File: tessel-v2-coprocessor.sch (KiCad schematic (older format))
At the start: 12 parts

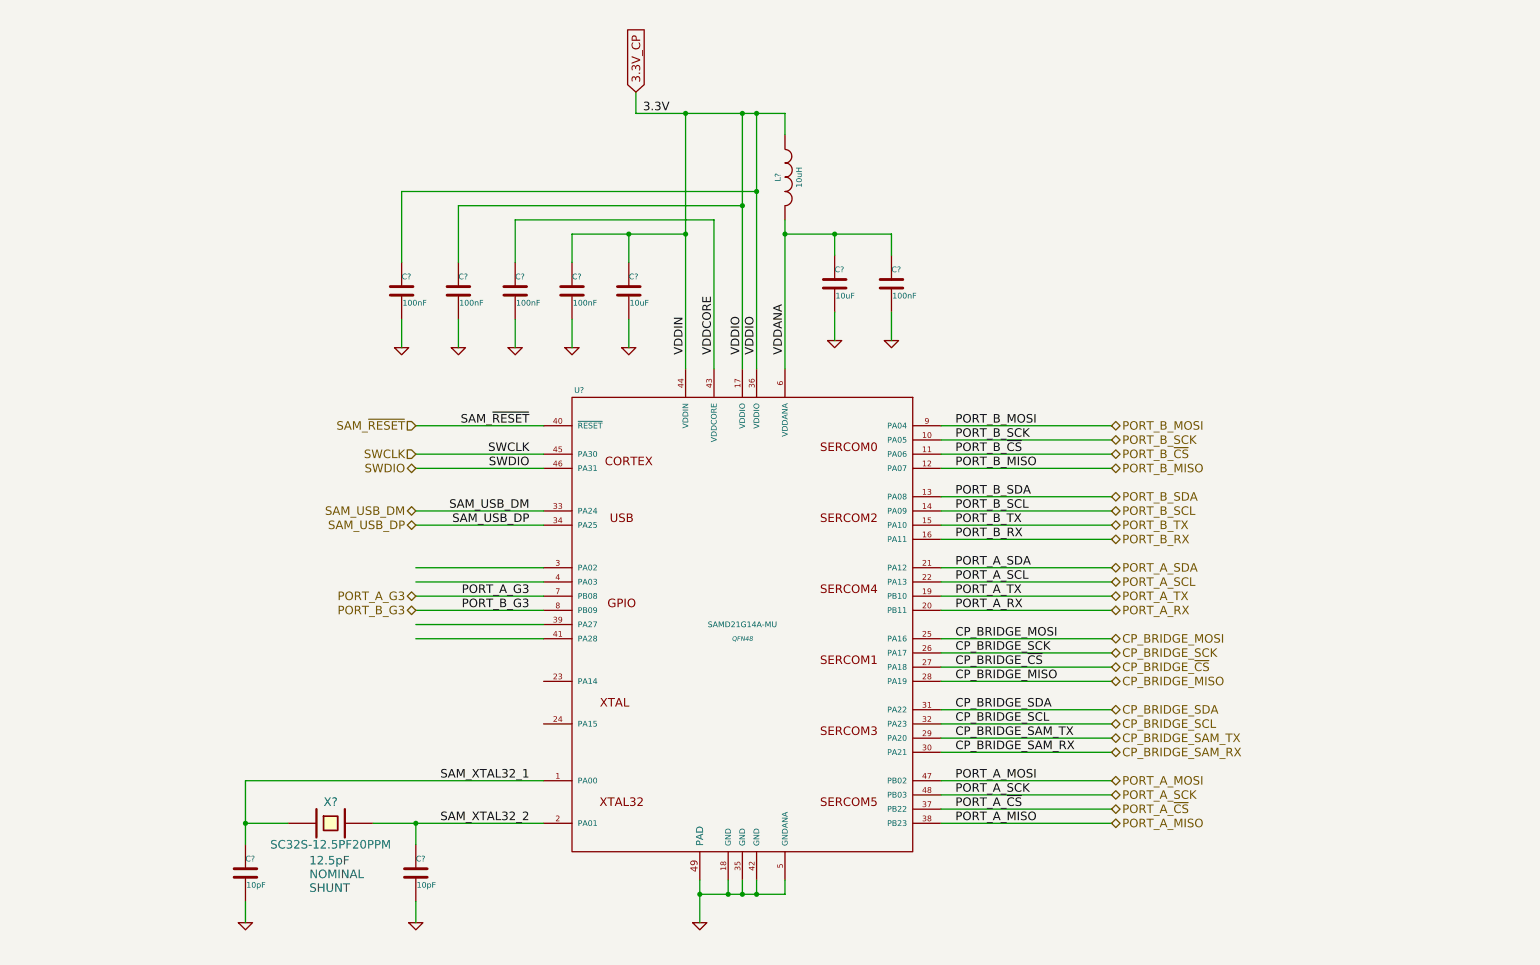
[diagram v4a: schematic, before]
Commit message: labels and series R for MT comms
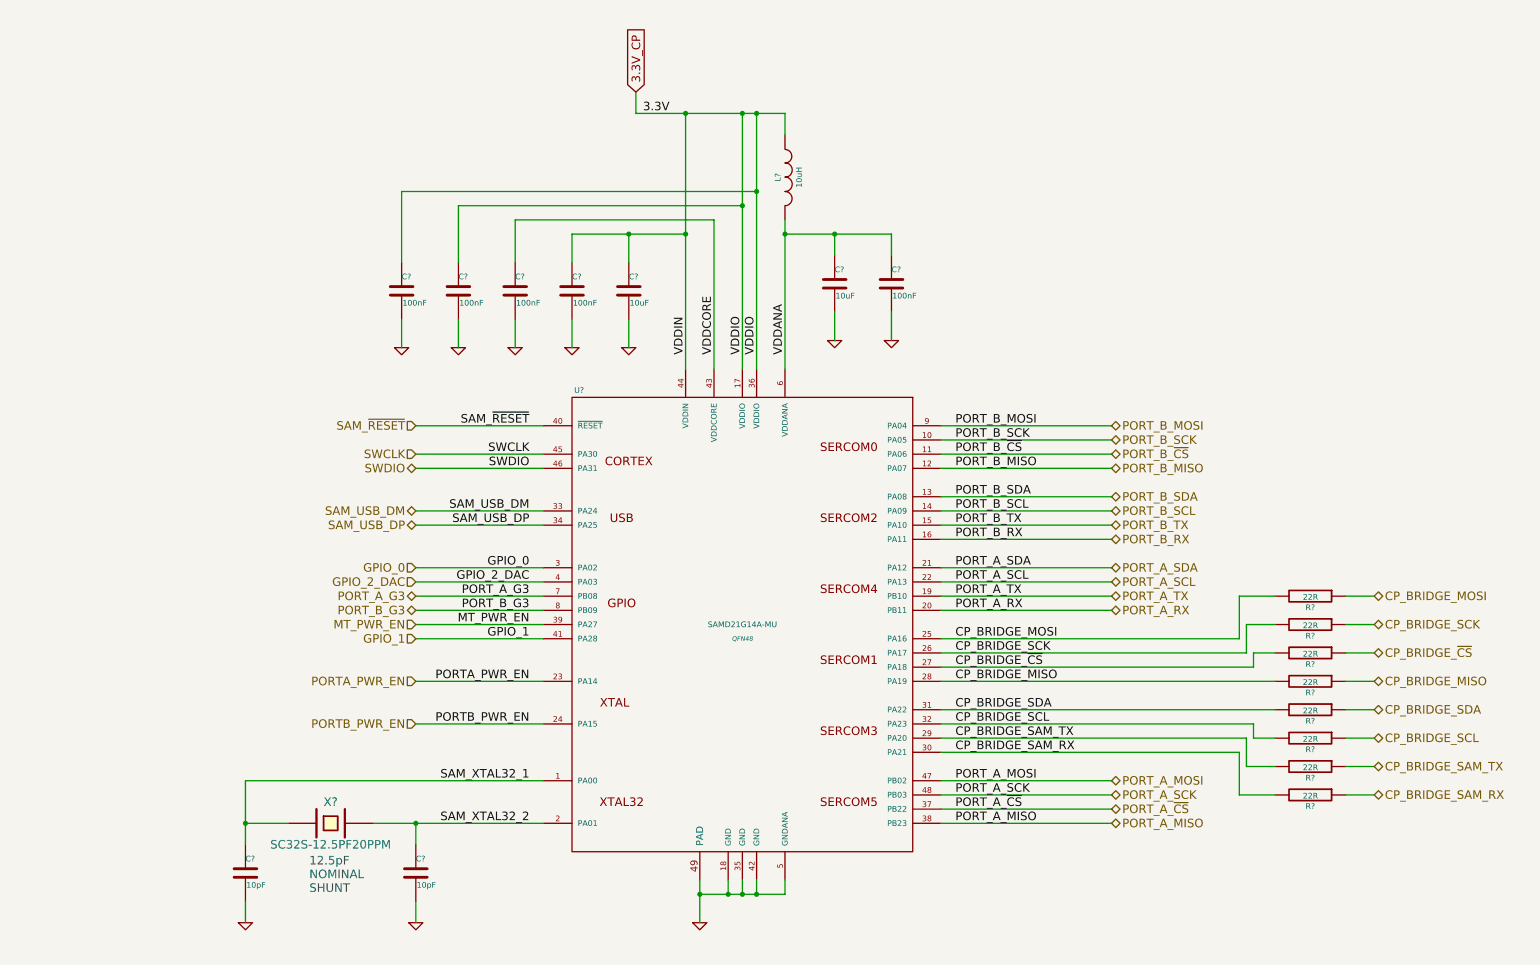
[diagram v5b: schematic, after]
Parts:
- added R? (x8): 22R, symbol R
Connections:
- net labels added: GPIO_0, GPIO_1, GPIO_2_DAC, MT_PWR_EN, PORTA_PWR_EN, PORTB_PWR_EN
- wire segments 90 -> 97
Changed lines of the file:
@@
 Text HLabel 10900 5900 2    60   BiDi ~ 0
 PORT_A_RX
-Text HLabel 10900 6100 2    60   BiDi ~ 0
+Text HLabel 12750 5800 2    60   BiDi ~ 0
 CP_BRIDGE_MOSI
-Text HLabel 10900 6200 2    60   BiDi ~ 0
+Text HLabel 12750 6000 2    60   BiDi ~ 0
 CP_BRIDGE_SCK
-Text HLabel 10900 6300 2    60   BiDi ~ 0
+Text HLabel 12750 6200 2    60   BiDi ~ 0
 CP_BRIDGE_~CS
-Text HLabel 10900 6400 2    60   BiDi ~ 0
+Text HLabel 12750 6400 2    60   BiDi ~ 0
 CP_BRIDGE_MISO
-Text HLabel 10900 6600 2    60   BiDi ~ 0
+Text HLabel 12750 6600 2    60   BiDi ~ 0
 CP_BRIDGE_SDA
-Text HLabel 10900 6700 2    60   BiDi ~ 0
+Text HLabel 12750 6800 2    60   BiDi ~ 0
 CP_BRIDGE_SCL
-Text HLabel 10900 6800 2    60   BiDi ~ 0
+Text HLabel 12750 7000 2    60   BiDi ~ 0
 CP_BRIDGE_SAM_TX
-Text HLabel 10900 6900 2    60   BiDi ~ 0
+Text HLabel 12750 7200 2    60   BiDi ~ 0
 CP_BRIDGE_SAM_RX
 Text HLabel 10900 7100 2    60   BiDi ~ 0
@@
 Connection ~ 7900 2400
 Wire Wire Line
-	7900 2400 7900 3250
-Wire Wire Line
-	7900 3250 7900 4200
+	7900 2400 7900 4200
 Connection ~ 8300 3050
 Connection ~ 8300 2400
@@
 Connection ~ 8400 2400
 Wire Wire Line
-	8400 2400 8400 2950
-Wire Wire Line
-	8400 2950 8400 4200
+	8400 2400 8400 4200
 Wire Wire Line
 	7550 2400 7550 2250
@@
 	8300 3050 6300 3050
 Wire Wire Line
-	8300 2400 8300 3050
-Wire Wire Line
-	8300 3050 8300 4200
+	8300 2400 8300 4200
 Wire Wire Line
 	8100 3150 8100 4200
@@
 	7100 3250 7100 3450
 Wire Wire Line
-	7100 3250 7500 3250
-Wire Wire Line
-	7500 3250 7900 3250
+	7100 3250 7900 3250
 Connection ~ 8600 3250
 Connection ~ 8950 3250
@@
 	8950 3250 8950 3400
 Wire Wire Line
-	8600 3250 8950 3250
-Wire Wire Line
-	8950 3250 9350 3250
-Wire Wire Line
-	8600 3150 8600 3250
-Wire Wire Line
-	8600 3250 8600 4200
+	8600 3250 9350 3250
+Wire Wire Line
+	8600 3150 8600 4200
 Wire Wire Line
 	4800 7950 4800 8100
@@
 	4800 7400 5100 7400
 Wire Wire Line
-	4800 7100 4800 7400
-Wire Wire Line
-	4800 7400 4800 7550
+	4800 7100 4800 7550
 Wire Wire Line
 	9700 7100 10900 7100
@@
 	9700 7200 10900 7200
 Wire Wire Line
-	9700 6900 10900 6900
-Wire Wire Line
-	9700 6800 10900 6800
-Wire Wire Line
-	9700 6700 10900 6700
-Wire Wire Line
-	9700 6600 10900 6600
-Wire Wire Line
-	9700 6400 10900 6400
-Wire Wire Line
-	9700 6300 10900 6300
-Wire Wire Line
-	9700 6200 10900 6200
-Wire Wire Line
-	9700 6100 10900 6100
+	9700 6400 12050 6400
+Wire Wire Line
+	9700 6300 11900 6300
+Wire Wire Line
+	9700 6200 11850 6200
+Wire Wire Line
+	9700 6100 11800 6100
 Wire Wire Line
 	9700 5900 10900 5900
@@
 	9700 4600 10900 4600
 Wire Wire Line
-	5700 7400 6000 7400
-Wire Wire Line
-	6000 7400 6900 7400
+	5700 7400 6900 7400
 Wire Wire Line
 	4800 7100 6900 7100
@@
 	6900 4600 6000 4600
 Wire Wire Line
-	7550 2400 7900 2400
-Wire Wire Line
-	7900 2400 8300 2400
-Wire Wire Line
-	8300 2400 8400 2400
-Wire Wire Line
-	8400 2400 8600 2400
+	7550 2400 8600 2400
 Wire Wire Line
 	7500 3450 7500 3250
@@
 $EndComp
 Wire Wire Line
-	8000 7800 8000 7900
-Wire Wire Line
-	8000 7900 8000 8100
-Wire Wire Line
-	8000 7900 8200 7900
-Wire Wire Line
-	8200 7900 8300 7900
-Wire Wire Line
-	8300 7900 8400 7900
-Wire Wire Line
-	8400 7900 8600 7900
+	8000 7800 8000 8100
+Wire Wire Line
+	8000 7900 8600 7900
 Wire Wire Line
 	8200 7900 8200 7800
@@
 Text GLabel 7550 2250 1    60   Input ~ 0
 3.3V_CP
+Text HLabel 6000 6400 0    60   Input ~ 0
+PORTA_PWR_EN
+Text HLabel 6000 6700 0    60   Input ~ 0
+PORTB_PWR_EN
+Text HLabel 6000 6000 0    60   Input ~ 0
+MT_PWR_EN
+$Comp
+L R R?
+U 1 1 54912B30
+P 12300 6200
+F 0 "R?" V 12380 6200 40  0000 C CNN
+F 1 "22R" V 12307 6201 40  0000 C CNN
+F 2 "" V 12230 6200 30  0000 C CNN
+F 3 "" H 12300 6200 30  0000 C CNN
+	1    12300 6200
+	0    1    1    0
+$EndComp
+$Comp
+L R R?
+U 1 1 54912C7C
+P 12300 6400
+F 0 "R?" V 12380 6400 40  0000 C CNN
+F 1 "22R" V 12307 6401 40  0000 C CNN
+F 2 "" V 12230 6400 30  0000 C CNN
+F 3 "" H 12300 6400 30  0000 C CNN
+	1    12300 6400
+	0    1    1    0
+$EndComp
+$Comp
+L R R?
+U 1 1 54912D2C
+P 12300 5800
+F 0 "R?" V 12380 5800 40  0000 C CNN
+F 1 "22R" V 12307 5801 40  0000 C CNN
+F 2 "" V 12230 5800 30  0000 C CNN
+F 3 "" H 12300 5800 30  0000 C CNN
+	1    12300 5800
+	0    1    1    0
+$EndComp
+$Comp
+L R R?
+U 1 1 54912D32
+P 12300 6000
+F 0 "R?" V 12380 6000 40  0000 C CNN
+F 1 "22R" V 12307 6001 40  0000 C CNN
+F 2 "" V 12230 6000 30  0000 C CNN
+F 3 "" H 12300 6000 30  0000 C CNN
+	1    12300 6000
+	0    1    1    0
+$EndComp
+Wire Wire Line
+	11850 6200 11850 6000
+Wire Wire Line
+	11850 6000 12050 6000
+Wire Wire Line
+	11900 6300 11900 6200
+Wire Wire Line
+	12050 5800 11800 5800
+Wire Wire Line
+	11800 5800 11800 6100
+Wire Wire Line
+	12550 5800 12750 5800
+Wire Wire Line
+	12750 6000 12550 6000
+Wire Wire Line
+	12550 6200 12750 6200
+Wire Wire Line
+	12750 6400 12550 6400
+Wire Wire Line
+	11900 6200 12050 6200
+Wire Wire Line
+	9700 6600 12050 6600
+Wire Wire Line
+	9700 6700 11900 6700
+Wire Wire Line
+	9700 6800 11850 6800
+Wire Wire Line
+	9700 6900 11800 6900
+$Comp
+L R R?
+U 1 1 54913EBE
+P 12300 6800
+F 0 "R?" V 12380 6800 40  0000 C CNN
+F 1 "22R" V 12307 6801 40  0000 C CNN
+F 2 "" V 12230 6800 30  0000 C CNN
+F 3 "" H 12300 6800 30  0000 C CNN
+	1    12300 6800
+	0    1    1    0
+$EndComp
+$Comp
+L R R?
+U 1 1 54913EC4
+P 12300 6600
+F 0 "R?" V 12380 6600 40  0000 C CNN
+F 1 "22R" V 12307 6601 40  0000 C CNN
+F 2 "" V 12230 6600 30  0000 C CNN
+F 3 "" H 12300 6600 30  0000 C CNN
+	1    12300 6600
+	0    1    1    0
+$EndComp
+$Comp
+L R R?
+U 1 1 54913ECA
+P 12300 7200
+F 0 "R?" V 12380 7200 40  0000 C CNN
+F 1 "22R" V 12307 7201 40  0000 C CNN
+F 2 "" V 12230 7200 30  0000 C CNN
+F 3 "" H 12300 7200 30  0000 C CNN
+	1    12300 7200
+	0    1    1    0
+$EndComp
+$Comp
+L R R?
+U 1 1 54913ED0
+P 12300 7000
+F 0 "R?" V 12380 7000 40  0000 C CNN
+F 1 "22R" V 12307 7001 40  0000 C CNN
+F 2 "" V 12230 7000 30  0000 C CNN
+F 3 "" H 12300 7000 30  0000 C CNN
+	1    12300 7000
+	0    1    1    0
+$EndComp
+Wire Wire Line
+	11850 6800 11850 7000
+Wire Wire Line
+	11850 7000 12050 7000
+Wire Wire Line
+	11900 6700 11900 6800
+Wire Wire Line
+	12050 7200 11800 7200
+Wire Wire Line
+	11800 7200 11800 6900
+Wire Wire Line
+	11900 6800 12050 6800
+Wire Wire Line
+	12550 6600 12750 6600
+Wire Wire Line
+	12750 6800 12550 6800
+Wire Wire Line
+	12550 7000 12750 7000
+Wire Wire Line
+	12550 7200 12750 7200
+Text Label 6800 5700 2    60   ~ 0
+GPIO_2_DAC
+Text Label 6800 5600 2    60   ~ 0
+GPIO_0
+Text Label 6800 6100 2    60   ~ 0
+GPIO_1
+Text Label 6800 6000 2    60   ~ 0
+MT_PWR_EN
+Text Label 6800 6400 2    60   ~ 0
+PORTA_PWR_EN
+Text Label 6800 6700 2    60   ~ 0
+PORTB_PWR_EN
+Wire Wire Line
+	6900 6400 6000 6400
+Wire Wire Line
+	6000 6700 6900 6700
+Text HLabel 6000 5600 0    60   Input ~ 0
+GPIO_0
+Text HLabel 6000 6100 0    60   Input ~ 0
+GPIO_1
+Text HLabel 6000 5700 0    60   Input ~ 0
+GPIO_2_DAC
 $EndSCHEMATC

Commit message: io pins, jtag, cortex, high level pins
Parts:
- added C?: 100nF, symbol C
- added R?: 22R, symbol R
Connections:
- net 3.3V_CP: now also R?.2
- net GND: now also C?.2
- net SAM_~RESET: now also C?.1, R?.1
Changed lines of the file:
@@
 Connection ~ 7900 2400
 Wire Wire Line
-	7900 2400 7900 4200
+	7900 2400 7900 3250
+Wire Wire Line
+	7900 3250 7900 4200
 Connection ~ 8300 3050
 Connection ~ 8300 2400
@@
 Connection ~ 8400 2400
 Wire Wire Line
-	8400 2400 8400 4200
+	8400 2400 8400 2950
+Wire Wire Line
+	8400 2950 8400 4200
 Wire Wire Line
 	7550 2400 7550 2250
@@
 	8300 3050 6300 3050
 Wire Wire Line
-	8300 2400 8300 4200
+	8300 2400 8300 3050
+Wire Wire Line
+	8300 3050 8300 4200
 Wire Wire Line
 	8100 3150 8100 4200
@@
 	7100 3250 7100 3450
 Wire Wire Line
-	7100 3250 7900 3250
+	7100 3250 7500 3250
+Wire Wire Line
+	7500 3250 7900 3250
 Connection ~ 8600 3250
 Connection ~ 8950 3250
@@
 	8950 3250 8950 3400
 Wire Wire Line
-	8600 3250 9350 3250
-Wire Wire Line
-	8600 3150 8600 4200
+	8600 3250 8950 3250
+Wire Wire Line
+	8950 3250 9350 3250
+Wire Wire Line
+	8600 3150 8600 3250
+Wire Wire Line
+	8600 3250 8600 4200
 Wire Wire Line
 	4800 7950 4800 8100
@@
 	4800 7400 5100 7400
 Wire Wire Line
-	4800 7100 4800 7550
+	4800 7100 4800 7400
+Wire Wire Line
+	4800 7400 4800 7550
 Wire Wire Line
 	9700 7100 10900 7100
@@
 	9700 4600 10900 4600
 Wire Wire Line
-	5700 7400 6900 7400
+	5700 7400 6000 7400
+Wire Wire Line
+	6000 7400 6900 7400
 Wire Wire Line
 	4800 7100 6900 7100
@@
 	6900 4600 6000 4600
 Wire Wire Line
-	7550 2400 8600 2400
+	7550 2400 7900 2400
+Wire Wire Line
+	7900 2400 8300 2400
+Wire Wire Line
+	8300 2400 8400 2400
+Wire Wire Line
+	8400 2400 8600 2400
 Wire Wire Line
 	7500 3450 7500 3250
@@
 $EndComp
 Wire Wire Line
-	8000 7800 8000 8100
-Wire Wire Line
-	8000 7900 8600 7900
+	8000 7800 8000 7900
+Wire Wire Line
+	8000 7900 8000 8100
+Wire Wire Line
+	8000 7900 8200 7900
+Wire Wire Line
+	8200 7900 8300 7900
+Wire Wire Line
+	8300 7900 8400 7900
+Wire Wire Line
+	8400 7900 8600 7900
 Wire Wire Line
 	8200 7900 8200 7800
@@
 Connection ~ 8400 7900
 Text Label 7600 2400 0    60   ~ 0
-3.3V
+3.3V_CP
 Text Label 8600 4100 1    60   ~ 0
 VDDANA
@@
 Text HLabel 6000 5700 0    60   Input ~ 0
 GPIO_2_DAC
+Text Label 3400 4600 0    60   ~ 0
+SAM_~RESET
+Wire Wire Line
+	3300 4600 4100 4600
+$Comp
+L C C?
+U 1 1 54978225
+P 4100 4900
+F 0 "C?" H 4100 5000 40  0000 L CNN
+F 1 "100nF" H 4106 4815 40  0000 L CNN
+F 2 "" H 4138 4750 30  0000 C CNN
+F 3 "" H 4100 4900 60  0000 C CNN
+	1    4100 4900
+	1    0    0    -1
+$EndComp
+Wire Wire Line
+	4100 4500 4100 4600
+Wire Wire Line
+	4100 4600 4100 4700
+Connection ~ 4100 4600
+Wire Wire Line
+	4100 5100 4100 5200
+$Comp
+L R R?
+U 1 1 5497863A
+P 4100 4250
+F 0 "R?" V 4180 4250 40  0000 C CNN
+F 1 "22R" V 4107 4251 40  0000 C CNN
+F 2 "" V 4030 4250 30  0000 C CNN
+F 3 "" H 4100 4250 30  0000 C CNN
+	1    4100 4250
+	-1   0    0    1
+$EndComp
+Wire Wire Line
+	4100 4000 4100 3900
+Text GLabel 4100 3900 1    60   Input ~ 0
+3.3V_CP
+$Comp
+L GND #PWR?
+U 1 1 54978E0E
+P 4100 5200
+F 0 "#PWR?" H 4100 5200 30  0001 C CNN
+F 1 "GND" H 4100 5130 30  0001 C CNN
+F 2 "" H 4100 5200 60  0000 C CNN
+F 3 "" H 4100 5200 60  0000 C CNN
+	1    4100 5200
+	1    0    0    -1
+$EndComp
 $EndSCHEMATC

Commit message: wiring up more i/o to cp
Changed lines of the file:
@@
 Connection ~ 7900 2400
 Wire Wire Line
-	7900 2400 7900 3250
-Wire Wire Line
-	7900 3250 7900 4200
+	7900 2400 7900 4200
 Connection ~ 8300 3050
 Connection ~ 8300 2400
@@
 Connection ~ 8400 2400
 Wire Wire Line
-	8400 2400 8400 2950
-Wire Wire Line
-	8400 2950 8400 4200
+	8400 2400 8400 4200
 Wire Wire Line
 	7550 2400 7550 2250
@@
 	8300 3050 6300 3050
 Wire Wire Line
-	8300 2400 8300 3050
-Wire Wire Line
-	8300 3050 8300 4200
+	8300 2400 8300 4200
 Wire Wire Line
 	8100 3150 8100 4200
@@
 	7100 3250 7100 3450
 Wire Wire Line
-	7100 3250 7500 3250
-Wire Wire Line
-	7500 3250 7900 3250
+	7100 3250 7900 3250
 Connection ~ 8600 3250
 Connection ~ 8950 3250
@@
 	8950 3250 8950 3400
 Wire Wire Line
-	8600 3250 8950 3250
-Wire Wire Line
-	8950 3250 9350 3250
-Wire Wire Line
-	8600 3150 8600 3250
-Wire Wire Line
-	8600 3250 8600 4200
+	8600 3250 9350 3250
+Wire Wire Line
+	8600 3150 8600 4200
 Wire Wire Line
 	4800 7950 4800 8100
@@
 	4800 7400 5100 7400
 Wire Wire Line
-	4800 7100 4800 7400
-Wire Wire Line
-	4800 7400 4800 7550
+	4800 7100 4800 7550
 Wire Wire Line
 	9700 7100 10900 7100
@@
 	9700 4600 10900 4600
 Wire Wire Line
-	5700 7400 6000 7400
-Wire Wire Line
-	6000 7400 6900 7400
+	5700 7400 6900 7400
 Wire Wire Line
 	4800 7100 6900 7100
@@
 	6900 4600 6000 4600
 Wire Wire Line
-	7550 2400 7900 2400
-Wire Wire Line
-	7900 2400 8300 2400
-Wire Wire Line
-	8300 2400 8400 2400
-Wire Wire Line
-	8400 2400 8600 2400
+	7550 2400 8600 2400
 Wire Wire Line
 	7500 3450 7500 3250
@@
 $EndComp
 Wire Wire Line
-	8000 7800 8000 7900
-Wire Wire Line
-	8000 7900 8000 8100
-Wire Wire Line
-	8000 7900 8200 7900
-Wire Wire Line
-	8200 7900 8300 7900
-Wire Wire Line
-	8300 7900 8400 7900
-Wire Wire Line
-	8400 7900 8600 7900
+	8000 7800 8000 8100
+Wire Wire Line
+	8000 7900 8600 7900
 Wire Wire Line
 	8200 7900 8200 7800
@@
 SAM_~RESET
 Wire Wire Line
-	3300 4600 4100 4600
+	3150 4600 4100 4600
 $Comp
 L C C?
@@
 $EndComp
 Wire Wire Line
-	4100 4500 4100 4600
-Wire Wire Line
-	4100 4600 4100 4700
+	4100 4500 4100 4700
 Connection ~ 4100 4600
 Wire Wire Line
